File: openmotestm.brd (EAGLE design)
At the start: 24.4 x 34 mm, 46 parts, among them X1 PHB_1MM27_2X05_SNS

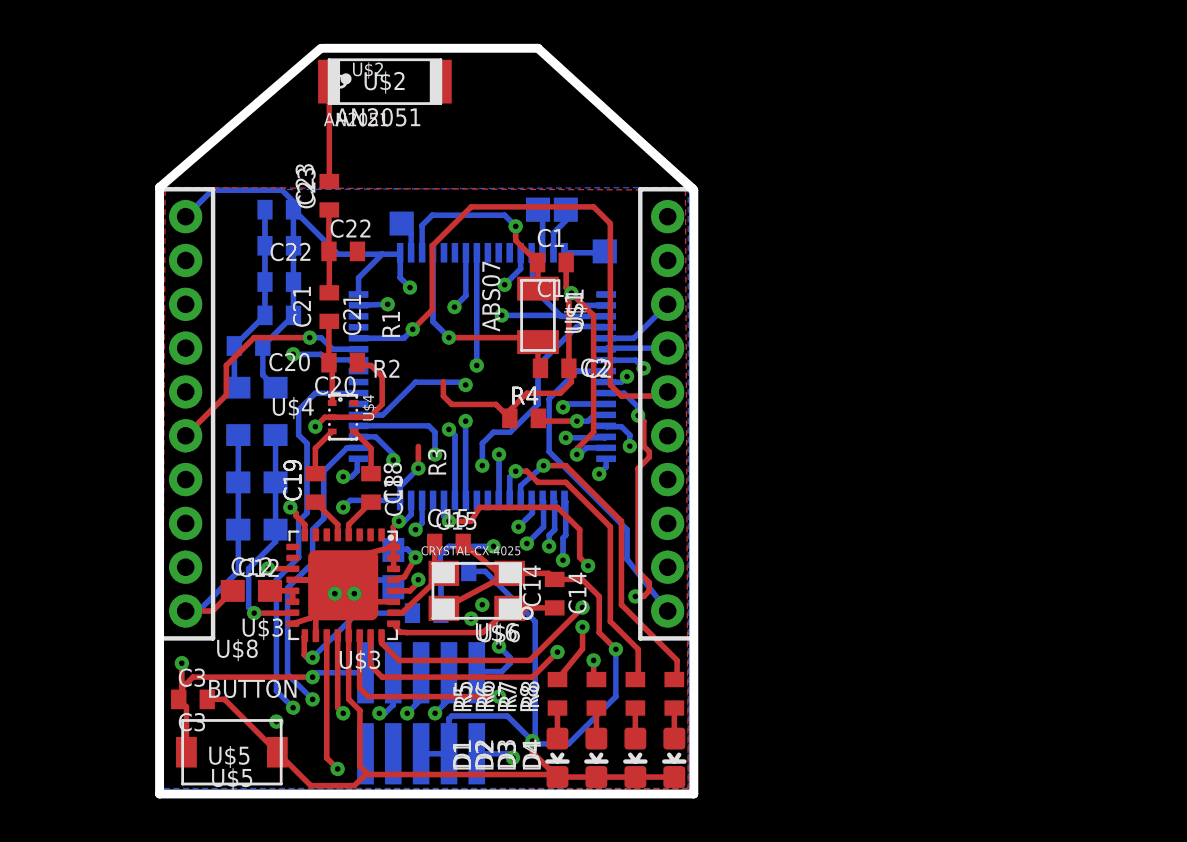
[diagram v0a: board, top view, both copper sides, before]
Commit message: Fix the package of chips.
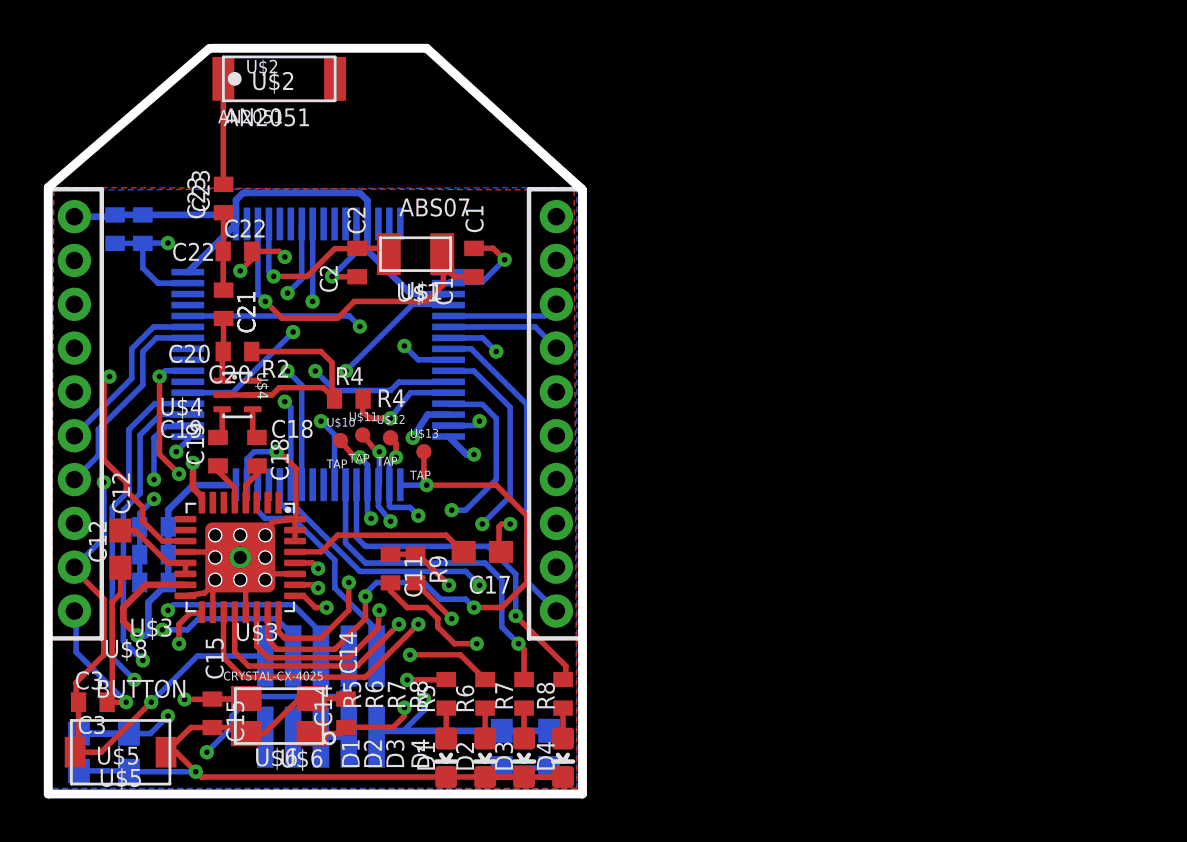
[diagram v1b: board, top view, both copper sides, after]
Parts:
- removed U$19, U$20, U$21, U$9: TAP, openmotestm:TAP
- added U$10, U$11, U$12, U$13: TAP, openmotestm:TAP
- moved C13 19.9 mm to (4.19, -9.40), turned to 270 degrees
- moved C16 16.7 mm to (6.35, -9.40), turned to 270 degrees
- moved C10 16.6 mm to (-15.1, -9.53), turned to 270 degrees
- moved C9 13.6 mm to (-12.8, -9.53), turned to 270 degrees
- moved C15 13.3 mm to (-9.02, -7.75), turned to 270 degrees
- moved C6 12.6 mm to (-11.7, 0.76)
- moved C7 12.3 mm to (-11.7, -0.51)
- moved C8 11.6 mm to (-11.7, -1.78)
- moved C14 11.0 mm to (-2.92, -7.75)
- moved U$6 10.7 mm to (-5.97, -7.87)
- moved C2 10.2 mm to (-2.41, 12.8), turned to 90 degrees
- moved R4 8.05 mm to (-2.79, 6.60)
- moved U$7 7.56 mm to (-4.19, 8.64)
- moved C4 7.55 mm to (-13.5, 14.4), turned to 270 degrees
- moved C5 6.27 mm to (-12.2, 14.4), turned to 270 degrees
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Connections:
- removed net PA0: U$21.P$1, U$7.14
- removed net PA1: U$20.P$1, U$7.15
- removed net PA2: U$19.P$1, U$7.16
- removed net PC13: U$7.2, U$9.P$1
- net RF_/SEL: now also U$13.P$1
- net RF_MISO: now also U$11.P$1
- net RF_MOSI: now also U$10.P$1
- net RF_SCLK: now also U$12.P$1
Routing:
- net GND: track 157.6 -> 144.0 mm, vias 10 -> 13
- net PC10: track 18.3 -> 29.7 mm, vias 3 -> 2
- net N$5: track 6.72 -> 18.0 mm, vias 1 -> 2
- net RF_/SEL: track 17.7 -> 27.1 mm, vias 2 -> 3
- net PC11: track 20.1 -> 29.6 mm, vias 3 -> 2
- net N$14: track 4.51 -> 13.5 mm, vias 0 -> 2
- net BOOT0: track 26.3 -> 18.3 mm
- net RF_CLKM: track 24.2 -> 16.3 mm, vias 3 -> 2
- net N$1: track 9.19 -> 15.8 mm
- net N$19: track 2.71 -> 8.33 mm, vias 1 -> 0
- net JTCK-SWCLK: track 24.5 -> 29.5 mm, vias 3 -> 2
- net N$7: track 7.98 -> 12.6 mm, vias 0 -> 2
- net RF_SLP_TR: track 21.9 -> 26.5 mm
- net RF_SCLK: track 26.4 -> 22.1 mm, vias 2 -> 3
- net PC12: track 17.4 -> 21.6 mm
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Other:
- board text removed: "R1"

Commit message: Revert "Fix the package of crystal-CX4025"
This reverts commit 4aa64b79fca5c8ea969664931983d918d7a77836.
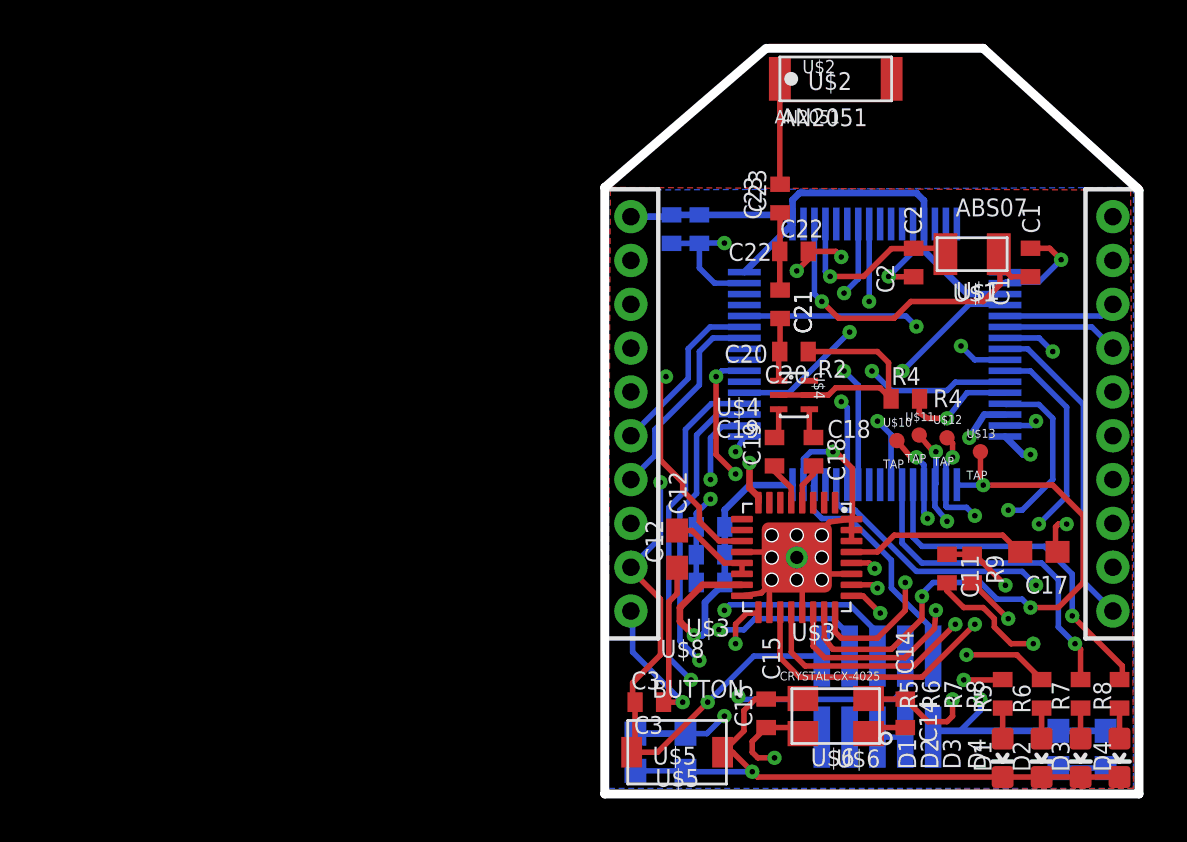
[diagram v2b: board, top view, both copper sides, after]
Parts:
- moved C14 25.5 mm to (22.6, -7.75), turned to 270 degrees
- moved C1 25.4 mm to (28.3, 12.8)
- moved C13 25.4 mm to (29.6, -9.40)
- moved C17 25.4 mm to (28.7, -0.38)
- moved D2 25.4 mm to (28.8, -9.78)
- moved R4 25.4 mm to (22.6, 6.60)
- moved R6 25.4 mm to (28.8, -6.86)
- moved U$10 25.4 mm to (22.2, 4.70)
- moved U$2 25.4 mm to (19.4, 21.2)
- moved U$6 25.4 mm to (19.4, -7.87)
- moved C10 25.4 mm to (10.3, -9.53)
- moved C11 25.4 mm to (24.5, -1.14)
- moved C12 25.4 mm to (12.2, -0.25)
- moved C16 25.4 mm to (31.8, -9.40)
- moved C18 25.4 mm to (18.4, 4.19)
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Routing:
- net JTCK-SWCLK: track 29.5 -> 24.6 mm
- net GND: track 144.0 -> 141.6 mm
- net N$14: track 13.5 -> 15.7 mm

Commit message: remove taps.
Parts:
- removed U$10, U$11, U$12, U$13: TAP, openmotestm:TAP
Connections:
- net RF_/SEL: no longer U$13.P$1
- net RF_MISO: no longer U$11.P$1
- net RF_MOSI: no longer U$10.P$1
- net RF_SCLK: no longer U$12.P$1
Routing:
- net RF_/SEL: track 27.1 -> 25.7 mm
- net RF_MISO: track 19.7 -> 18.7 mm
- net RF_MOSI: track 17.2 -> 16.2 mm
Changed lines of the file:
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@@
 </element>
 <element name="X1" library="_hhn_con_pinhead_box_1mm27" package="PHB_1MM27_2X05_SNS" value="PHB_1MM27_2X05_SNS" x="21.336" y="-6.985" rot="MR0"/>
-<element name="U$10" library="openmotestm" package="TAP" value="TAP" x="22.225" y="4.699"/>
-<element name="U$11" library="openmotestm" package="TAP" value="TAP" x="23.241" y="4.953"/>
-<element name="U$12" library="openmotestm" package="TAP" value="TAP" x="24.511" y="4.826"/>
-<element name="U$13" library="openmotestm" package="TAP" value="TAP" x="26.035" y="4.191"/>
 </elements>
 <signals>
@@
 <contactref element="U$3" pad="22"/>
 <contactref element="U$7" pad="36"/>
-<contactref element="U$10" pad="P$1"/>
 <wire x1="18.403" y1="-3.135" x2="18.403" y2="-4.687" width="0.254" layer="1"/>
 <wire x1="18.403" y1="-4.687" x2="18.923" y2="-5.207" width="0.254" layer="1"/>
@@
 <via x="23.114" y="3.937" extent="1-16" drill="0.254" diameter="0.4064"/>
 <wire x1="23.114" y1="3.937" x2="22.86" y2="3.937" width="0.254" layer="1"/>
-<wire x1="22.86" y1="3.937" x2="22.225" y2="4.699" width="0.254" layer="1"/>
 </signal>
 <signal name="RF_MISO">
 <contactref element="U$3" pad="20"/>
 <contactref element="U$7" pad="35"/>
-<contactref element="U$11" pad="P$1"/>
 <wire x1="17.403" y1="-3.135" x2="17.403" y2="-4.957" width="0.254" layer="1"/>
 <wire x1="17.403" y1="-4.957" x2="18.034" y2="-5.588" width="0.254" layer="1"/>
@@
 <wire x1="24.892" y1="0.635" x2="24.892" y2="-3.683" width="0.254" layer="2"/>
 <via x="24.892" y="-3.683" extent="1-16" drill="0.254" diameter="0.4064"/>
-<wire x1="23.241" y1="4.953" x2="23.876" y2="4.191" width="0.254" layer="1"/>
 <wire x1="23.876" y1="4.191" x2="24.003" y2="4.191" width="0.254" layer="1"/>
 <via x="24.003" y="4.191" extent="1-16" drill="0.254" diameter="0.4064"/>
@@
 <contactref element="U$3" pad="19"/>
 <contactref element="U$7" pad="34"/>
-<contactref element="U$12" pad="P$1"/>
 <wire x1="24.459" y1="2.686" x2="24.459" y2="3.631" width="0.254" layer="16"/>
 <wire x1="24.459" y1="3.631" x2="24.765" y2="3.937" width="0.254" layer="16"/>
 <via x="24.765" y="3.937" extent="1-16" drill="0.254" diameter="0.4064"/>
 <wire x1="24.765" y1="3.937" x2="24.765" y2="4.572" width="0.254" layer="1"/>
-<wire x1="24.765" y1="4.572" x2="24.511" y2="4.826" width="0.254" layer="1"/>
 <wire x1="24.459" y1="2.686" x2="24.459" y2="1.703" width="0.254" layer="16"/>
 <wire x1="24.459" y1="1.703" x2="24.511" y2="1.651" width="0.254" layer="16"/>
@@
 <contactref element="U$7" pad="33"/>
 <contactref element="U$3" pad="23"/>
-<contactref element="U$13" pad="P$1"/>
 <wire x1="18.903" y1="-3.135" x2="18.903" y2="-4.298" width="0.254" layer="1"/>
 <wire x1="18.903" y1="-4.298" x2="19.304" y2="-4.826" width="0.254" layer="1"/>
@@
 <wire x1="26.162" y1="2.667" x2="24.978" y2="2.667" width="0.254" layer="16"/>
 <wire x1="24.978" y1="2.667" x2="24.959" y2="2.686" width="0.254" layer="16"/>
-<wire x1="26.035" y1="4.191" x2="26.035" y2="2.794" width="0.254" layer="1"/>
 <wire x1="26.035" y1="2.794" x2="26.162" y2="2.667" width="0.254" layer="1"/>
 <wire x1="23.368" y1="-2.413" x2="23.368" y2="-3.429" width="0.254" layer="1"/>

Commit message: Fix place Layer.
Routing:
- net RF_SCLK: track 21.8 -> 19.8 mm, vias 3 -> 2
- net RF_MISO: track 18.7 -> 17.1 mm, vias 3 -> 2
- net RF_MOSI: track 16.2 -> 14.6 mm, vias 3 -> 2
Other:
- board text added: "C17"
- board text removed: "R2"
- board text removed: "R3"
